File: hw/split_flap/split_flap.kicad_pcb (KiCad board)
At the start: 2 copper layers, 104.5 x 98.3 mm, 50 parts, among them J1 Conn_01x02, J10 Conn_01x05, J11 Conn_01x05, J12 Conn_01x05, J13 Conn_01x05, J14 Conn_01x05, J15 Conn_01x05, J16 Conn_01x05, J17 EXPANDER_PORT, J18 Conn_01x05, J19 POWER, J2 Conn_01x02, J20 Conn_01x05, J21 Conn_01x05, J22 Conn_01x05, J23 Conn_01x02, J24 Conn_01x02, J25 Conn_01x02, J26 Conn_01x02, J3 Conn_01x02, J4 Conn_01x02, J5 Conn_01x02, J6 Conn_01x02, J7 Conn_01x02, J8 Conn_01x02, J9 Conn_01x05, U1 PCF8574, U10 ULN2803A, U11 PCF8574, U12 ULN2803A, U13 PCF8574, U14 ULN2803A, U2 NodeMCU_1.0_(ESP-12E), U3 PCF8574, U4 ULN2803A, U5 PCF8574, U6 ULN2803A, U7 PCF8574, U8 ULN2803A, U9 PCF8574

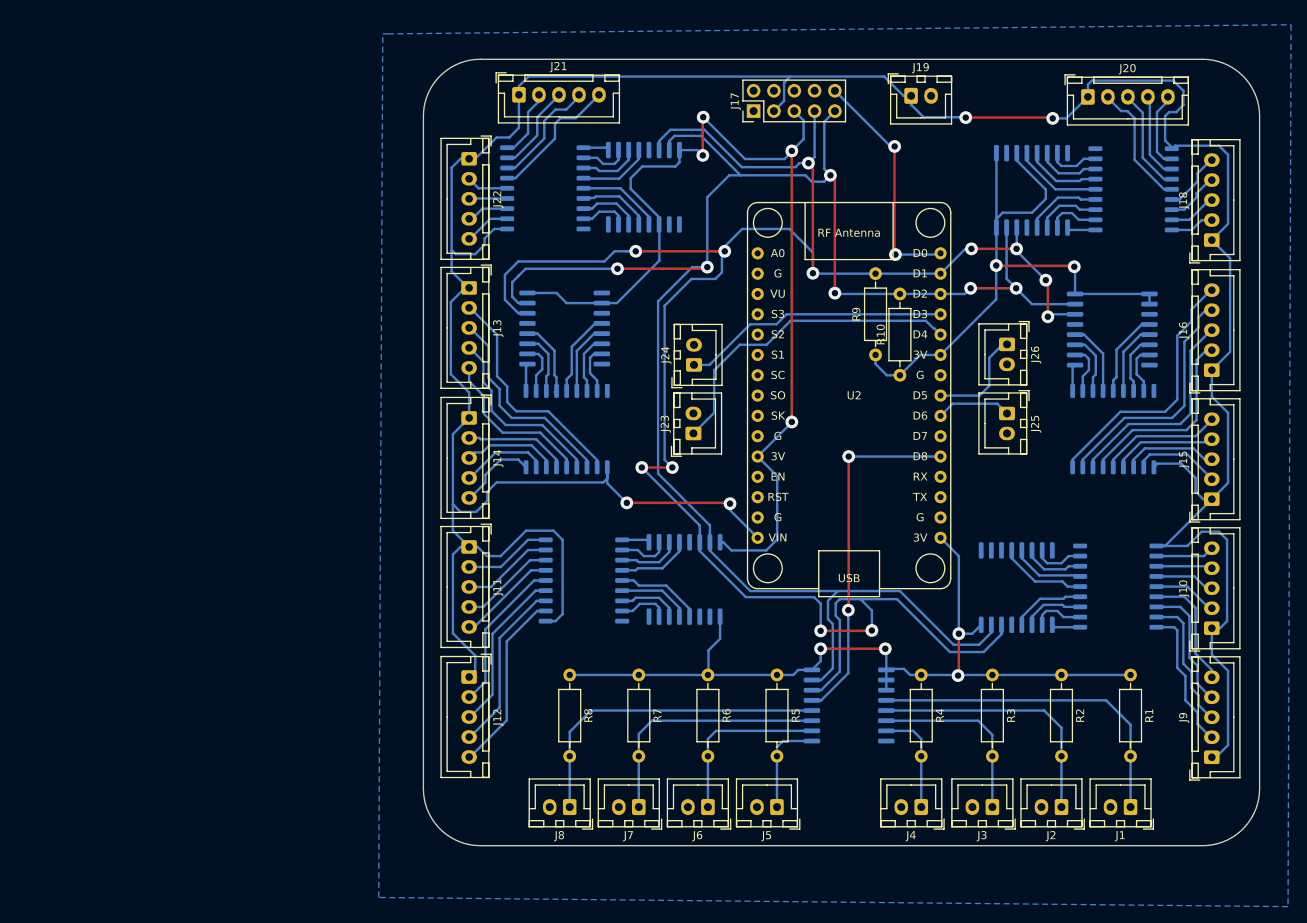
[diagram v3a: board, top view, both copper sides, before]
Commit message: hw: Route pcb completely
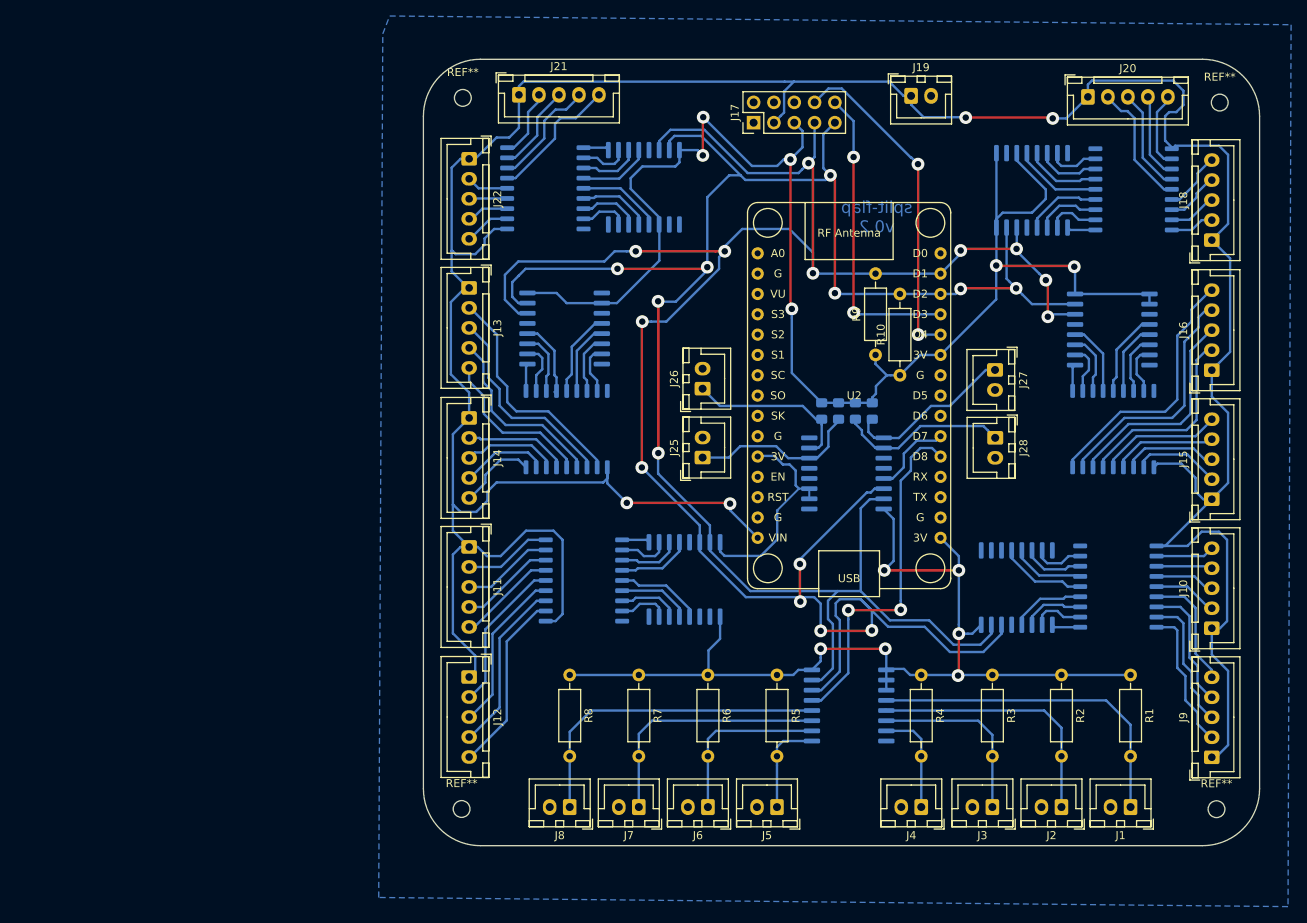
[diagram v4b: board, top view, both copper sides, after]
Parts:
- removed J23, J24: Conn_01x02, Connector_JST:JST_XH_B2B-XH-A_1x02_P2.50mm_Vertical
- added J27: Conn_01x02, Connector_JST:JST_XH_B2B-XH-A_1x02_P2.50mm_Vertical, F.Cu at (167.8, 80.0)
- added J28: Conn_01x02, Connector_JST:JST_XH_B2B-XH-A_1x02_P2.50mm_Vertical, F.Cu at (167.9, 88.5)
- added R13: R, Resistor_SMD:R_0805_2012Metric_Pad1.15x1.40mm_HandSolder, B.Cu at (148.3, 85.1)
- added R14: R, Resistor_SMD:R_0805_2012Metric_Pad1.15x1.40mm_HandSolder, B.Cu at (146.2, 85.1)
- added R15: R, Resistor_SMD:R_0805_2012Metric_Pad1.15x1.40mm_HandSolder, B.Cu at (152.5, 85.1)
- added R16: R, Resistor_SMD:R_0805_2012Metric_Pad1.15x1.40mm_HandSolder, B.Cu at (150.4, 85.1)
- added REF**: MountingHole_2.1mm, MountingHole:MountingHole_2.1mm, F.Cu at (101.3, 46.0)
- added REF**: MountingHole_2.1mm, MountingHole:MountingHole_2.1mm, F.Cu at (101.2, 134.9)
- added REF**: MountingHole_2.1mm, MountingHole:MountingHole_2.1mm, F.Cu at (195.5, 134.9)
- added REF**: MountingHole_2.1mm, MountingHole:MountingHole_2.1mm, F.Cu at (195.9, 46.6)
- added U15: PCF8574, Package_SO:SOIC-16W_7.5x10.3mm_P1.27mm, B.Cu at (149.3, 92.9)
- moved J26 38.4 mm to (131.3, 82.3), turned to 90 degrees
- moved J25 38.4 mm to (131.3, 90.9), turned to 90 degrees
- moved J17 1.45 mm to (137.7, 49.1)
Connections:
- net /INT renamed /INT1
- J17 pad 10: /EXP_INT -> /EXT_INT1
- J17 pad 8: (no net) -> /EXT_INT2
- J25 pad 1: /EXT_INT2 -> Net-(J25-Pad1)
- J26 pad 1: /EXT_INT1 -> Net-(J26-Pad1)
- U2 pad 21: (no net) -> /INT2
- U2 pad 22: /EXT_INT2 -> (no net)
- U2 pad 23: /EXT_INT1 -> (no net)
- U2 pad 26: /EXT_INT4 -> /EXT_INT2
- U2 pad 27: /EXT_INT3 -> /EXT_INT1
- U2 pad 30: /EXP_INT -> (no net)
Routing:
- net /EXT_INT4: track 40.5 -> 0.00 mm
- net /EXT_INT3: track 33.4 -> 0.00 mm
- net /EXT_INT2: track 9.44 -> 41.7 mm, vias 0 -> 2
- net /EXP_INT: track 29.6 -> 0.00 mm, vias 2 -> 0
- net +3V3: track 313.0 -> 341.1 mm, vias 10 -> 12
- net /EXT_INT1: track 13.0 -> 38.2 mm, vias 0 -> 2
- net Net-(J25-Pad1): track 0.00 -> 21.5 mm
- net Net-(J27-Pad1): track 0.00 -> 21.5 mm
- net Net-(J26-Pad1): track 0.00 -> 21.4 mm
- net Net-(J28-Pad1): track 0.00 -> 21.3 mm
- net /SCL: track 258.7 -> 275.6 mm, vias 12 -> 14
- net /SDA: track 227.7 -> 240.2 mm, vias 6 -> 8
- net /INT2: track 0.00 -> 10.3 mm
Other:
- board text added: "split-flap v0.2"

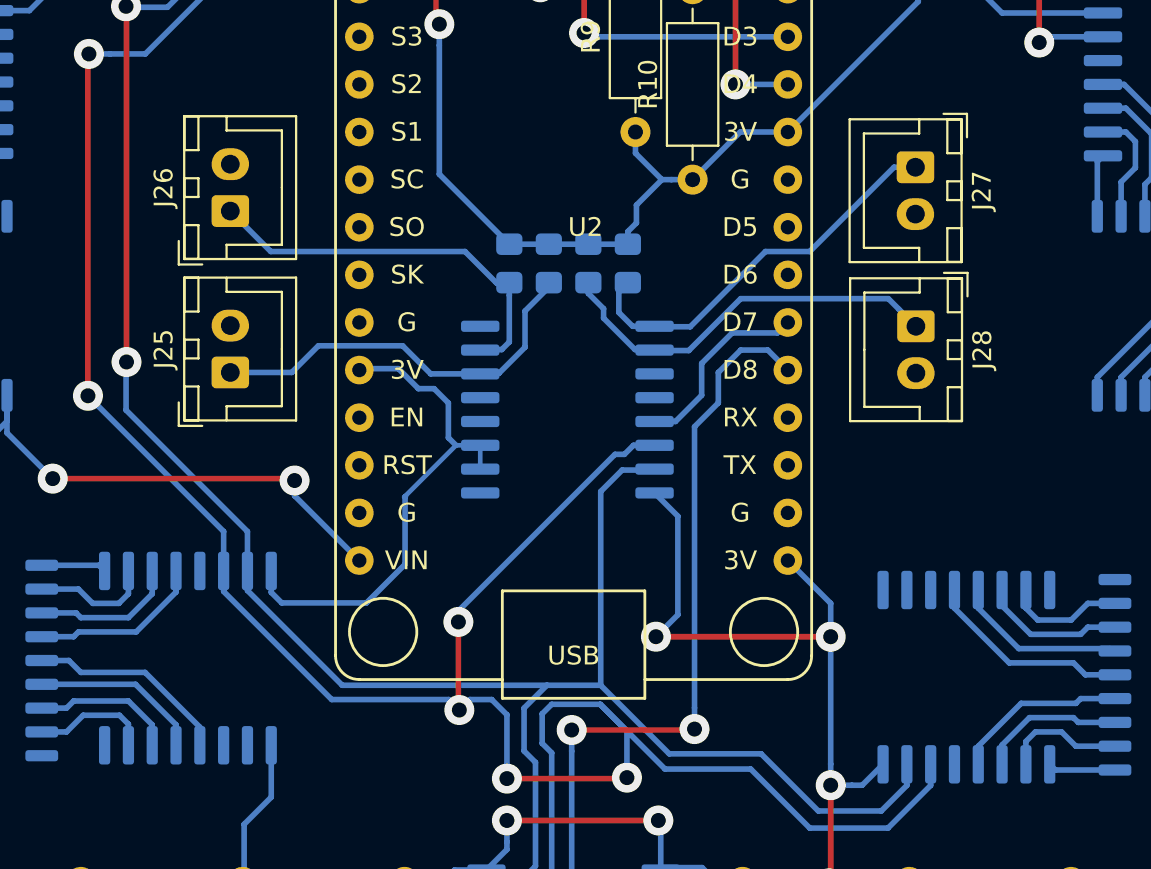
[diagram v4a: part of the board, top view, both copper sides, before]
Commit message: More spacing between esp and input connectors
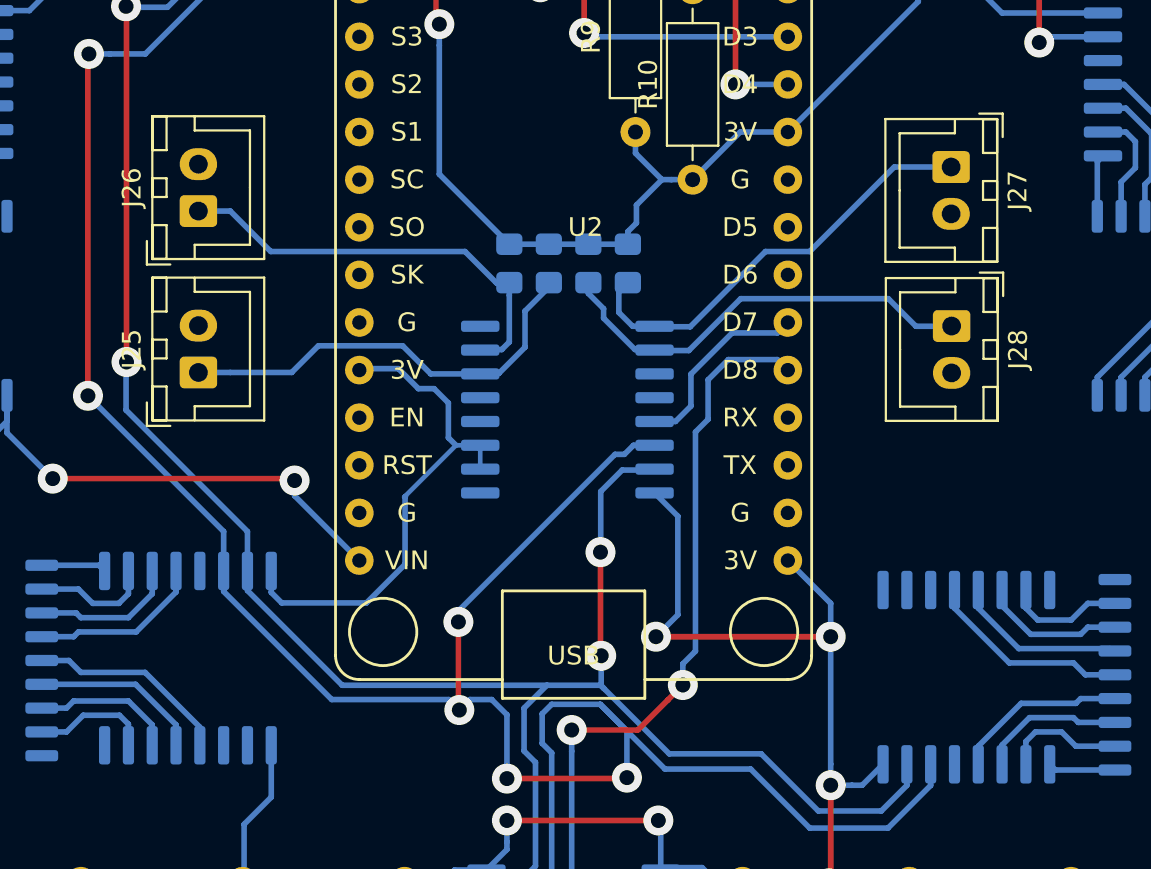
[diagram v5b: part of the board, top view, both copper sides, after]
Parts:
- moved J27 1.91 mm to (169.7, 80.0)
- moved J28 1.91 mm to (169.8, 88.5)
- moved J25 1.70 mm to (129.6, 90.9)
- moved J26 1.70 mm to (129.6, 82.3)
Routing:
- net /INT1: track 44.6 -> 42.5 mm
- net Net-(J27-Pad1): track 21.5 -> 23.4 mm
- net Net-(J28-Pad1): track 21.3 -> 23.2 mm
- net Net-(J26-Pad1): track 21.4 -> 23.1 mm
- net Net-(J25-Pad1): track 21.5 -> 23.2 mm
- net /SDA: track 240.2 -> 240.5 mm, vias 8 -> 10
